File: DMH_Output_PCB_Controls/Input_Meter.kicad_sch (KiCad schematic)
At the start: 29 parts, among them U20 TL072, U24 LM339, U25 LM339

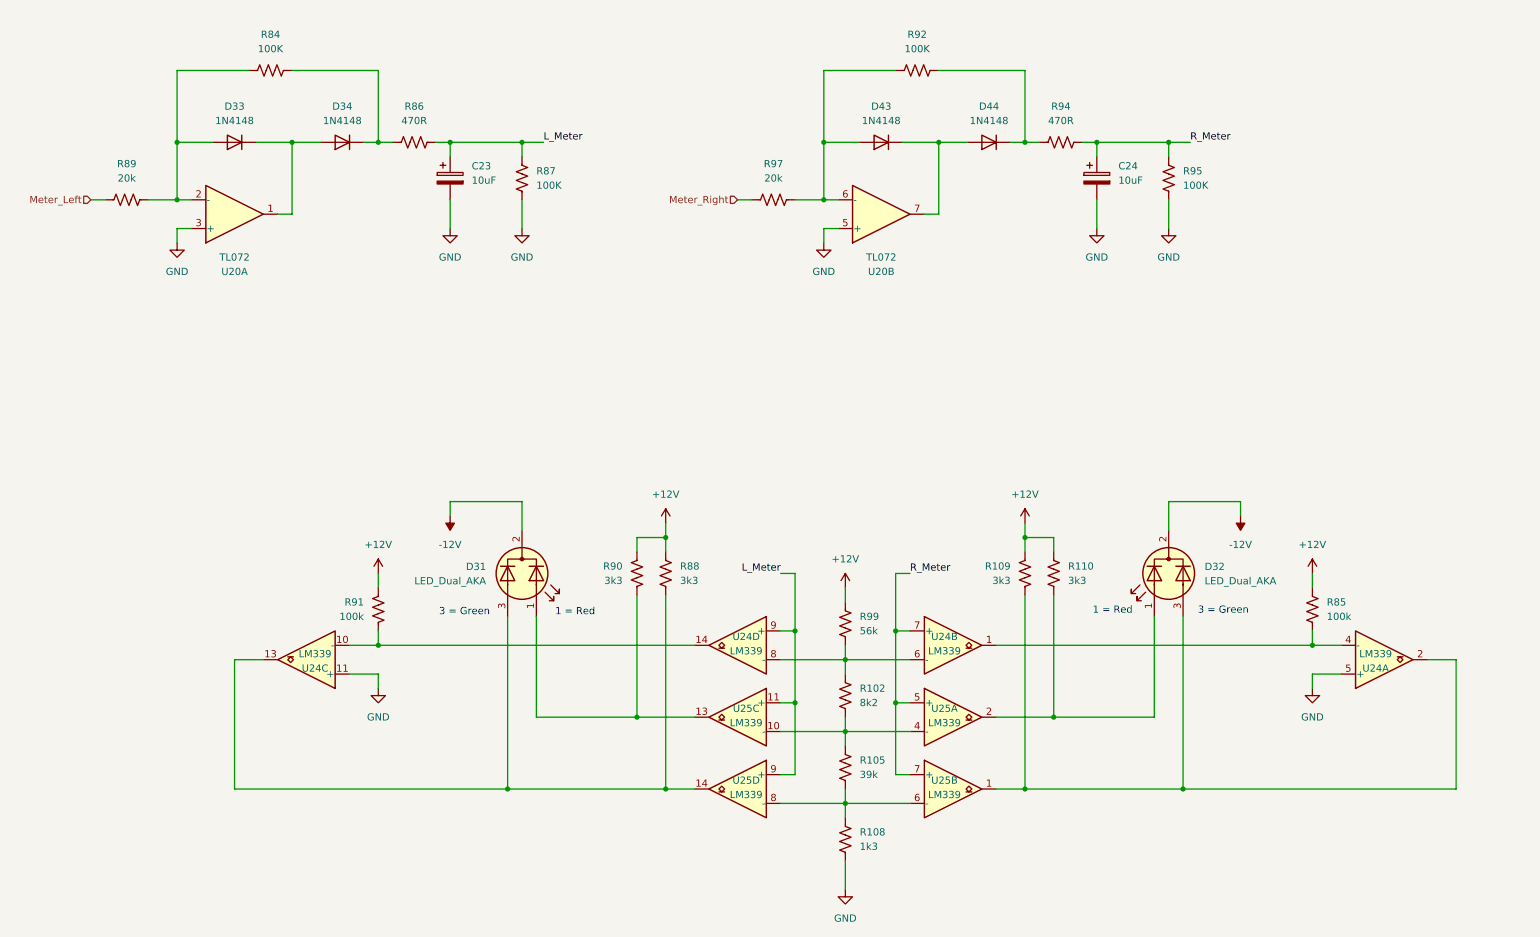
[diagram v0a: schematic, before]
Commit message: Adjusted meter circuits
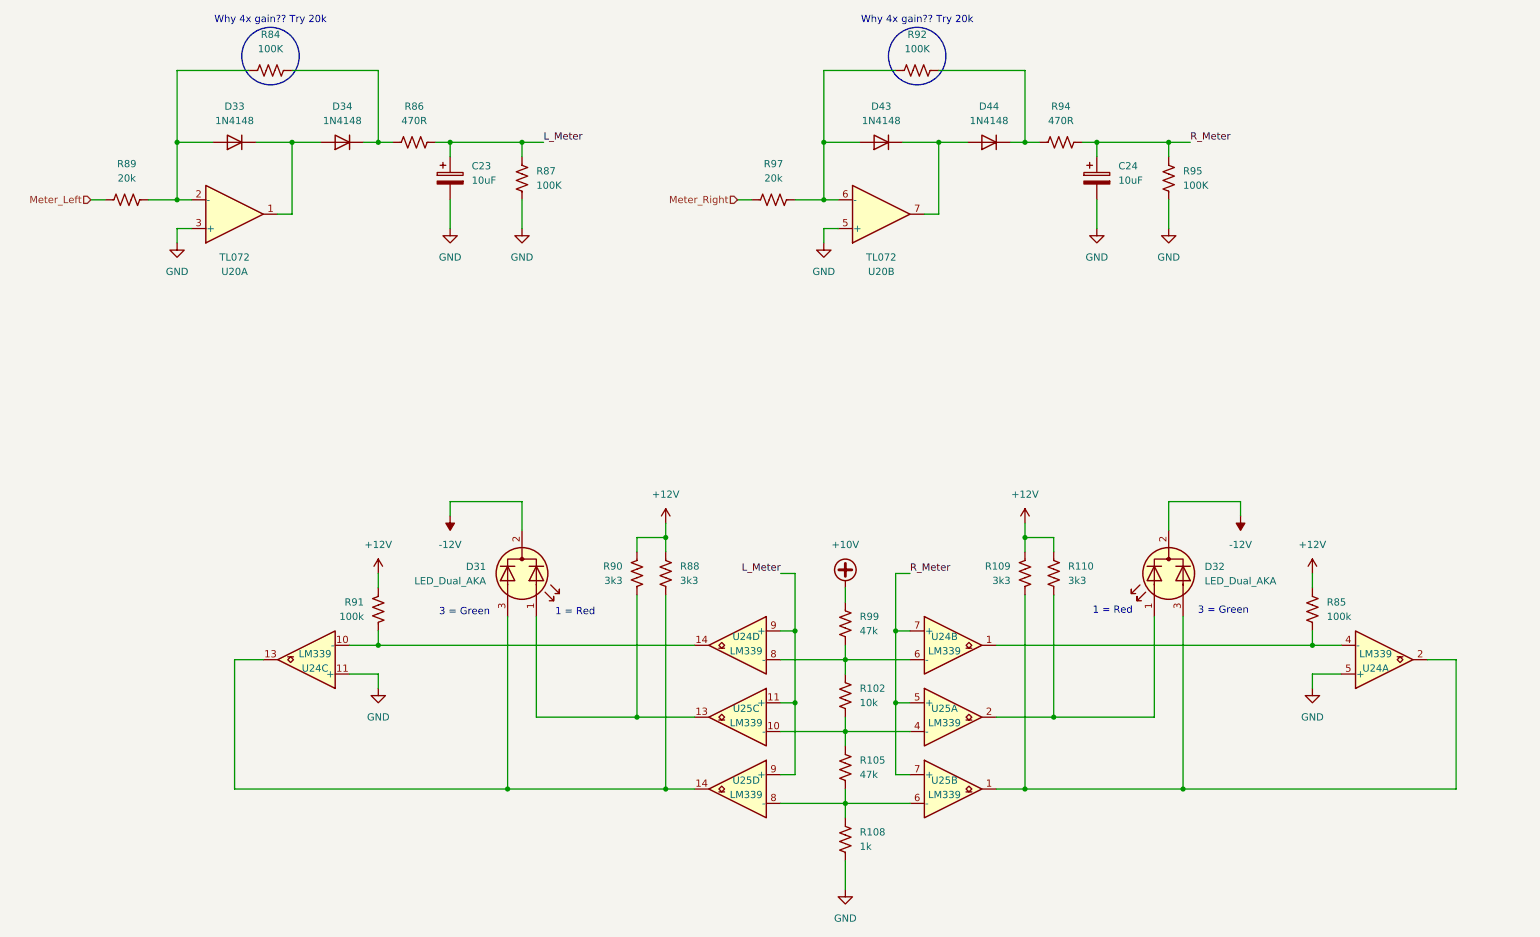
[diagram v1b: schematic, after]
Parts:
- R102: value 8k2 -> 10k
- R105: value 39k -> 47k
- R108: value 1k3 -> 1k
- R99: value 56k -> 47k
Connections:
- net +12V: no longer R99.2
- new net +10V: R99.2
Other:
- note added: "Why 4x gain?? Try 20k"
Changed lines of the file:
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@@
 		(comment 1 "PCB for 5 cm Kosmo format synthesizer module")
 	)
+	(circle
+		(center 57.15 22.86)
+		(radius 5.08)
+		(stroke
+			(width 0)
+			(type default)
+		)
+		(fill
+			(type none)
+		)
+	)
+	(circle
+		(center 171.45 22.86)
+		(radius 5.08)
+		(stroke
+			(width 0)
+			(type default)
+		)
+		(fill
+			(type none)
+		)
+	)
 	(text "3 = Green"
 		(exclude_from_sim no)
@@
 		)
 	)
+	(text "Why 4x gain?? Try 20k"
+		(exclude_from_sim no)
+		(at 57.15 16.51 0)
+		(effects
+			(font
+				(size 1.27 1.27)
+			)
+		)
+	)
 	(text "3 = Green"
 		(exclude_from_sim no)
@@
 		)
 	)
+	(text "Why 4x gain?? Try 20k"
+		(exclude_from_sim no)
+		(at 171.45 16.51 0)
+		(effects
+			(font
+				(size 1.27 1.27)
+			)
+		)
+	)
 	(text "1 = Red"
 		(exclude_from_sim no)
@@
 	)
 	(symbol
+		(lib_id "power:+VDC")
+		(at 158.75 116.84 0)
+		(unit 1)
+		(exclude_from_sim no)
+		(in_bom yes)
+		(on_board yes)
+		(dnp no)
+		(fields_autoplaced yes)
+		(property "Reference" "#PWR053"
+			(at 158.75 119.38 0)
+			(effects
+				(font
+					(size 1.27 1.27)
+				)
+				(hide yes)
+			)
+		)
+		(property "Value" "+10V"
+			(at 158.75 109.22 0)
+			(effects
+				(font
+					(size 1.27 1.27)
+				)
+			)
+		)
+		(property "Footprint" ""
+			(at 158.75 116.84 0)
+			(effects
+				(font
+					(size 1.27 1.27)
+				)
+				(hide yes)
+			)
+		)
+		(property "Datasheet" ""
+			(at 158.75 116.84 0)
+			(effects
+				(font
+					(size 1.27 1.27)
+				)
+				(hide yes)
+			)
+		)
+		(property "Description" "Power symbol creates a global label with name \"+VDC\""
+			(at 158.75 116.84 0)
+			(effects
+				(font
+					(size 1.27 1.27)
+				)
+				(hide yes)
+			)
+		)
+		(pin "1"
+		)
+		(instances
+			(project "DMH_Output_PCB_Controls"
+				(path "/58f4306d-5387-4983-bb08-41a2313fd315/55c0022e-9ebc-4247-b070-6524df6af06d"
+					(reference "#PWR053")
+					(unit 1)
+				)
+			)
+		)
+	)
+	(symbol
 		(lib_id "Device:R_US")
 		(at 195.58 114.3 180)
@@
 			)
 		)
-		(property "Value" "8k2"
+		(property "Value" "10k"
 			(at 161.29 137.1599 0)
 			(effects
@@
 			)
 		)
-		(property "Value" "39k"
+		(property "Value" "47k"
 			(at 161.29 149.8599 0)
 			(effects
@@
 	)
 	(symbol
-		(lib_id "power:+12V")
-		(at 158.75 116.84 0)
-		(unit 1)
-		(exclude_from_sim no)
-		(in_bom yes)
-		(on_board yes)
-		(dnp no)
-		(fields_autoplaced yes)
-		(property "Reference" "#PWR053"
-			(at 158.75 120.65 0)
-			(effects
-				(font
-					(size 1.27 1.27)
-				)
-				(hide yes)
-			)
-		)
-		(property "Value" "+12V"
-			(at 158.75 111.76 0)
-			(effects
-				(font
-					(size 1.27 1.27)
-				)
-			)
-		)
-		(property "Footprint" ""
-			(at 158.75 116.84 0)
-			(effects
-				(font
-					(size 1.27 1.27)
-				)
-				(hide yes)
-			)
-		)
-		(property "Datasheet" ""
-			(at 158.75 116.84 0)
-			(effects
-				(font
-					(size 1.27 1.27)
-				)
-				(hide yes)
-			)
-		)
-		(property "Description" "Power symbol creates a global label with name \"+12V\""
-			(at 158.75 116.84 0)
-			(effects
-				(font
-					(size 1.27 1.27)
-				)
-				(hide yes)
-			)
-		)
-		(pin "1"
-		)
-		(instances
-			(project "DMH_Output_PCB_1"
-				(path "/58f4306d-5387-4983-bb08-41a2313fd315/55c0022e-9ebc-4247-b070-6524df6af06d"
-					(reference "#PWR053")
-					(unit 1)
-				)
-			)
-		)
-	)
-	(symbol
 		(lib_id "Device:R_US")
 		(at 31.75 48.26 90)
@@
 			)
 		)
-		(property "Value" "56k"
+		(property "Value" "47k"
 			(at 161.29 124.4599 0)
 			(effects
@@
 			)
 		)
-		(property "Value" "1k3"
+		(property "Value" "1k"
 			(at 161.29 162.5599 0)
 			(effects

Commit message: Controls PCB placement ongoing
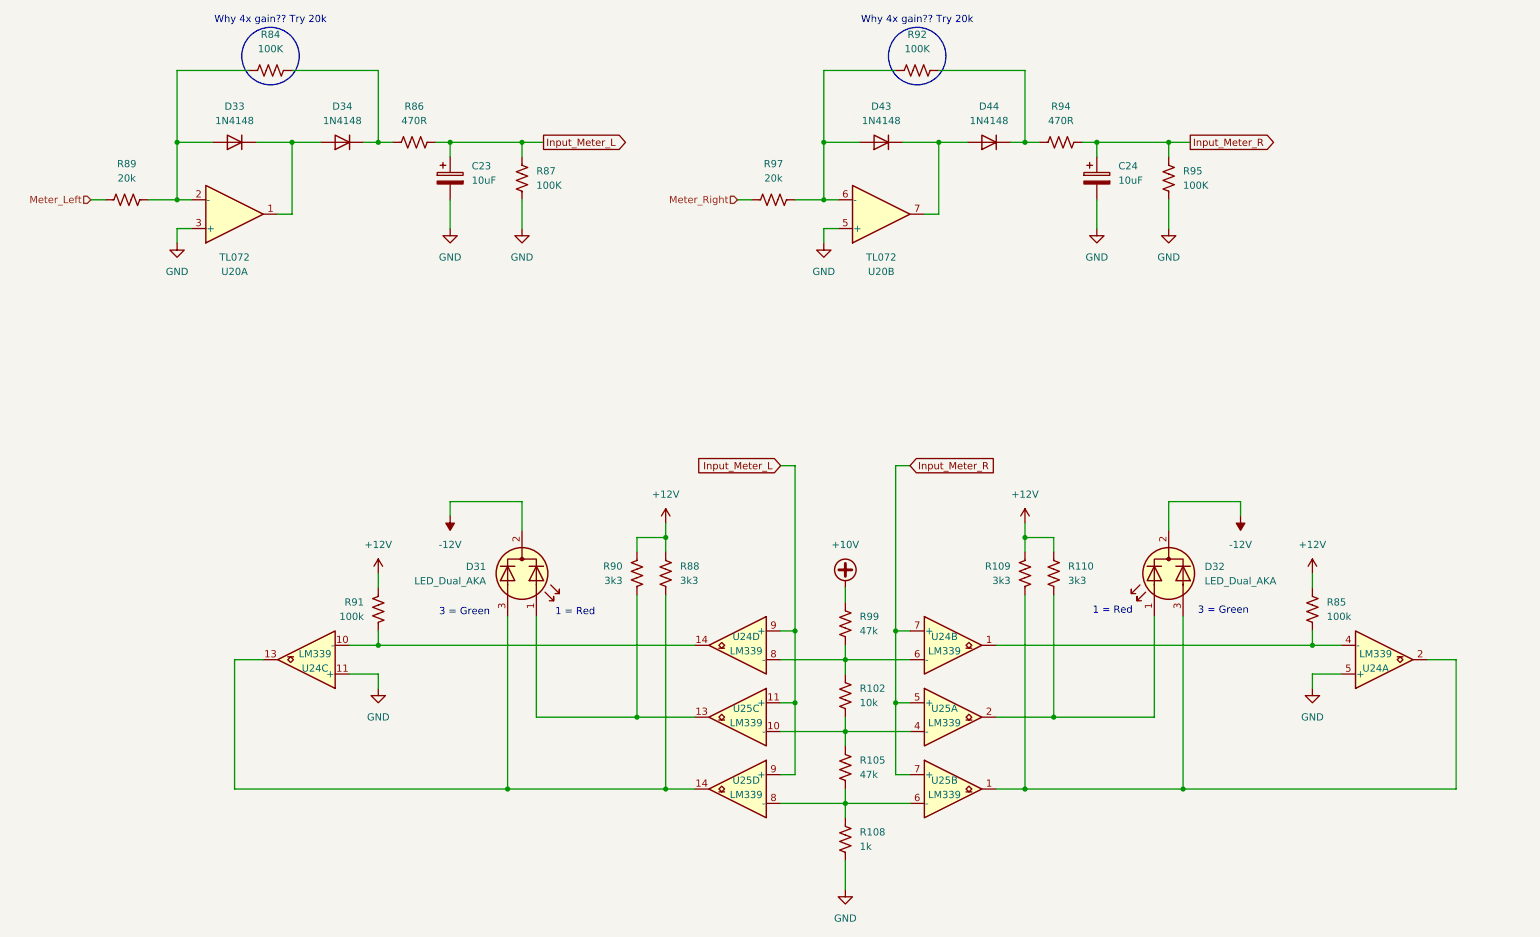
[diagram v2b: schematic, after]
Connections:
- net L_Meter renamed Input_Meter_L
- net R_Meter renamed Input_Meter_R
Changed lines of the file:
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@@
 	(wire
 		(pts
-			(xy 170.18 114.3) (xy 167.64 114.3)
+			(xy 170.18 95.25) (xy 167.64 95.25)
 		)
 		(stroke
@@
 	(wire
 		(pts
-			(xy 149.86 114.3) (xy 149.86 124.46)
+			(xy 149.86 95.25) (xy 149.86 124.46)
 		)
 		(stroke
@@
 	(wire
 		(pts
-			(xy 147.32 114.3) (xy 149.86 114.3)
+			(xy 147.32 95.25) (xy 149.86 95.25)
 		)
 		(stroke
@@
 	(wire
 		(pts
-			(xy 167.64 114.3) (xy 167.64 124.46)
+			(xy 167.64 95.25) (xy 167.64 124.46)
 		)
 		(stroke
@@
 		)
 	)
-	(label "L_Meter"
-		(at 147.32 114.3 180)
+	(global_label "Input_Meter_R"
+		(shape output)
+		(at 219.71 38.1 0)
+		(fields_autoplaced yes)
 		(effects
 			(font
 				(size 1.27 1.27)
 			)
-			(justify right bottom)
+			(justify left)
+		)
+		(property "Intersheetrefs" "${INTERSHEET_REFS}"
+			(at 235.8184 38.1 0)
+			(effects
+				(font
+					(size 1.27 1.27)
+				)
+				(justify left)
+				(hide yes)
+			)
 		)
 	)
-	(label "R_Meter"
-		(at 219.71 38.1 0)
+	(global_label "Input_Meter_R"
+		(shape input)
+		(at 170.18 95.25 0)
+		(fields_autoplaced yes)
 		(effects
 			(font
 				(size 1.27 1.27)
 			)
-			(justify left bottom)
+			(justify left)
+		)
+		(property "Intersheetrefs" "${INTERSHEET_REFS}"
+			(at 186.2884 95.25 0)
+			(effects
+				(font
+					(size 1.27 1.27)
+				)
+				(justify left)
+				(hide yes)
+			)
 		)
 	)
-	(label "L_Meter"
-		(at 105.41 38.1 0)
+	(global_label "Input_Meter_L"
+		(shape input)
+		(at 147.32 95.25 180)
+		(fields_autoplaced yes)
 		(effects
 			(font
 				(size 1.27 1.27)
 			)
-			(justify left bottom)
+			(justify right)
+		)
+		(property "Intersheetrefs" "${INTERSHEET_REFS}"
+			(at 131.4535 95.25 0)
+			(effects
+				(font
+					(size 1.27 1.27)
+				)
+				(justify right)
+				(hide yes)
+			)
 		)
 	)
-	(label "R_Meter"
-		(at 170.18 114.3 0)
+	(global_label "Input_Meter_L"
+		(shape output)
+		(at 105.41 38.1 0)
+		(fields_autoplaced yes)
 		(effects
 			(font
 				(size 1.27 1.27)
 			)
-			(justify left bottom)
+			(justify left)
+		)
+		(property "Intersheetrefs" "${INTERSHEET_REFS}"
+			(at 121.2765 38.1 0)
+			(effects
+				(font
+					(size 1.27 1.27)
+				)
+				(justify left)
+				(hide yes)
+			)
 		)
 	)
@@
 		(exclude_from_sim no)
 		(in_bom yes)
-		(on_board yes)
+		(on_board no)
 		(dnp no)
 		(fields_autoplaced yes)
@@
 		(exclude_from_sim no)
 		(in_bom yes)
-		(on_board yes)
+		(on_board no)
 		(dnp no)
 		(fields_autoplaced yes)
@@
 		(exclude_from_sim no)
 		(in_bom yes)
-		(on_board yes)
+		(on_board no)
 		(dnp no)
 		(fields_autoplaced yes)
@@
 		(exclude_from_sim no)
 		(in_bom yes)
-		(on_board yes)
+		(on_board no)
 		(dnp no)
 		(fields_autoplaced yes)
@@
 		(exclude_from_sim no)
 		(in_bom yes)
-		(on_board yes)
+		(on_board no)
 		(dnp no)
 		(fields_autoplaced yes)
@@
 		(exclude_from_sim no)
 		(in_bom yes)
-		(on_board yes)
+		(on_board no)
 		(dnp no)
 		(fields_autoplaced yes)
@@
 		(exclude_from_sim no)
 		(in_bom yes)
-		(on_board yes)
+		(on_board no)
 		(dnp no)
 		(fields_autoplaced yes)
@@
 		(exclude_from_sim no)
 		(in_bom yes)
-		(on_board yes)
+		(on_board no)
 		(dnp no)
 		(fields_autoplaced yes)
@@
 		(exclude_from_sim no)
 		(in_bom yes)
-		(on_board yes)
+		(on_board no)
 		(dnp no)
 		(fields_autoplaced yes)
@@
 		(exclude_from_sim no)
 		(in_bom yes)
-		(on_board yes)
+		(on_board no)
 		(dnp no)
 		(fields_autoplaced yes)
@@
 		(exclude_from_sim no)
 		(in_bom yes)
-		(on_board yes)
+		(on_board no)
 		(dnp no)
 		(fields_autoplaced yes)
@@
 		(exclude_from_sim no)
 		(in_bom yes)
-		(on_board yes)
+		(on_board no)
 		(dnp no)
 		(fields_autoplaced yes)
@@
 		(exclude_from_sim no)
 		(in_bom yes)
-		(on_board yes)
+		(on_board no)
 		(dnp no)
 		(fields_autoplaced yes)
@@
 		(exclude_from_sim no)
 		(in_bom yes)
-		(on_board yes)
+		(on_board no)
 		(dnp no)
 		(fields_autoplaced yes)
@@
 		(exclude_from_sim no)
 		(in_bom yes)
-		(on_board yes)
+		(on_board no)
 		(dnp no)
 		(fields_autoplaced yes)
@@
 		(exclude_from_sim no)
 		(in_bom yes)
-		(on_board yes)
+		(on_board no)
 		(dnp no)
 		(fields_autoplaced yes)
@@
 		(exclude_from_sim no)
 		(in_bom yes)
-		(on_board yes)
+		(on_board no)
 		(dnp no)
 		(fields_autoplaced yes)
@@
 		(exclude_from_sim no)
 		(in_bom yes)
-		(on_board yes)
+		(on_board no)
 		(dnp no)
 		(property "Reference" "U20"
@@
 		(exclude_from_sim no)
 		(in_bom yes)
-		(on_board yes)
+		(on_board no)
 		(dnp no)
 		(fields_autoplaced yes)
@@
 		(exclude_from_sim no)
 		(in_bom yes)
-		(on_board yes)
+		(on_board no)
 		(dnp no)
 		(fields_autoplaced yes)
@@
 		(exclude_from_sim no)
 		(in_bom yes)
-		(on_board yes)
+		(on_board no)
 		(dnp no)
 		(fields_autoplaced yes)
@@
 		(exclude_from_sim no)
 		(in_bom yes)
-		(on_board yes)
+		(on_board no)
 		(dnp no)
 		(property "Reference" "U20"

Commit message: Clarifying inter PCB connectors in progress
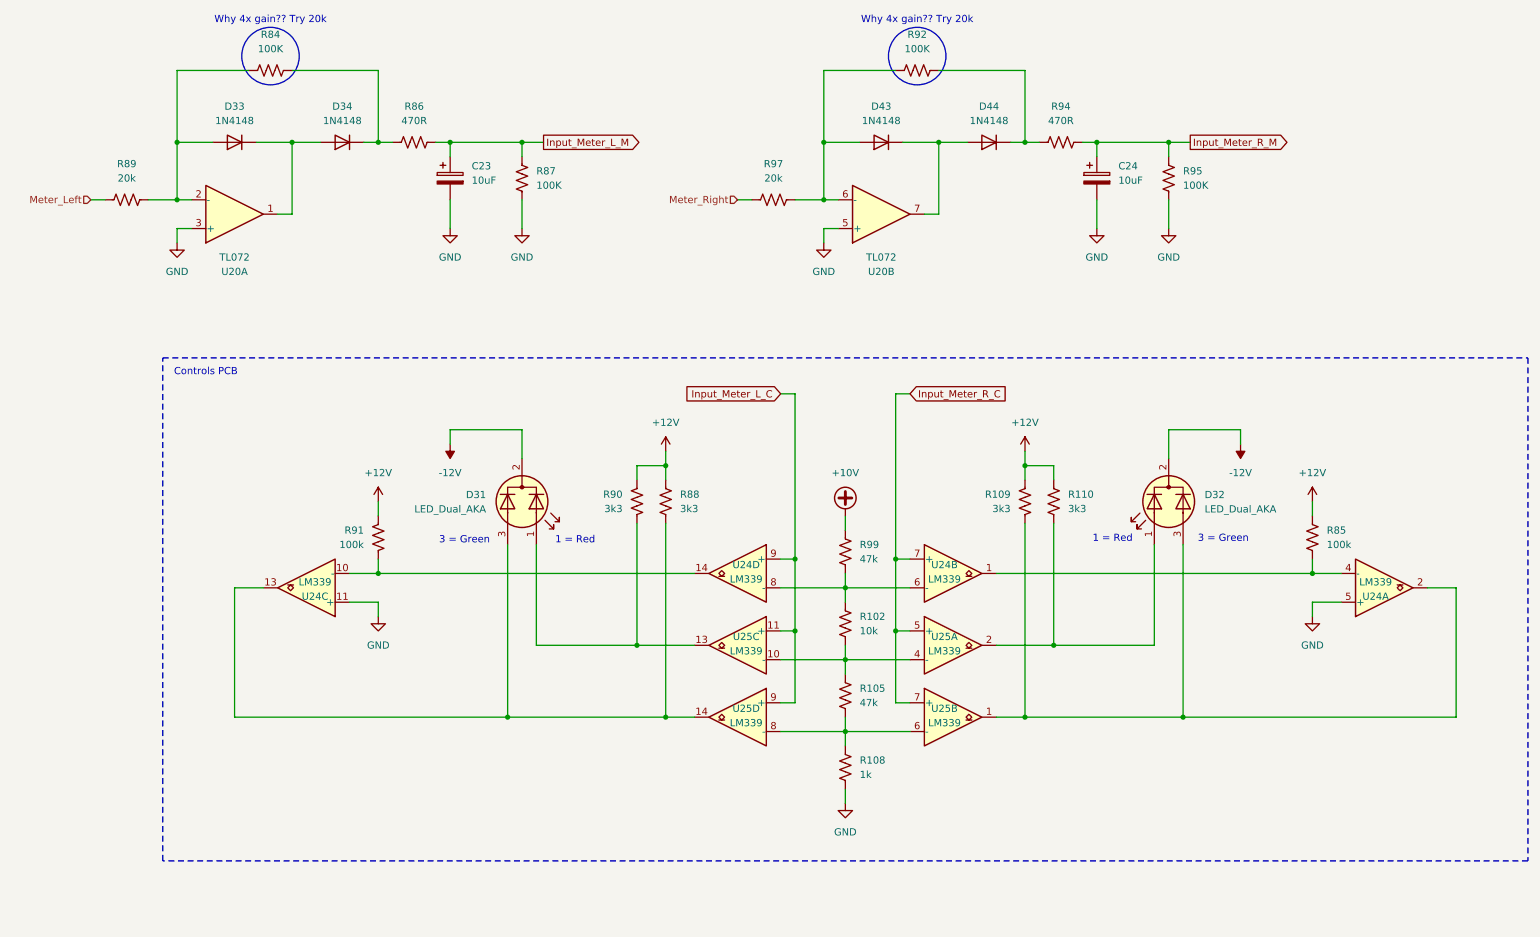
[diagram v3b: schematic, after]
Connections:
- net Input_Meter_L renamed Input_Meter_L_C
- net Input_Meter_L_C: no longer C23.1, R86.2, R87.2
- net Input_Meter_R renamed Input_Meter_R_C
- net Input_Meter_R_C: no longer C24.1, R94.2, R95.2
- new net Input_Meter_L_M: C23.1, R86.2, R87.2
- new net Input_Meter_R_M: C24.1, R94.2, R95.2
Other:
- note added: "Controls PCB"
- moved on the sheet: D31, D32, R102, R105, R108, R109, R110, R85, R88, R90, R91, R99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
